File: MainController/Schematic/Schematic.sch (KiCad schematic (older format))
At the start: 3 parts

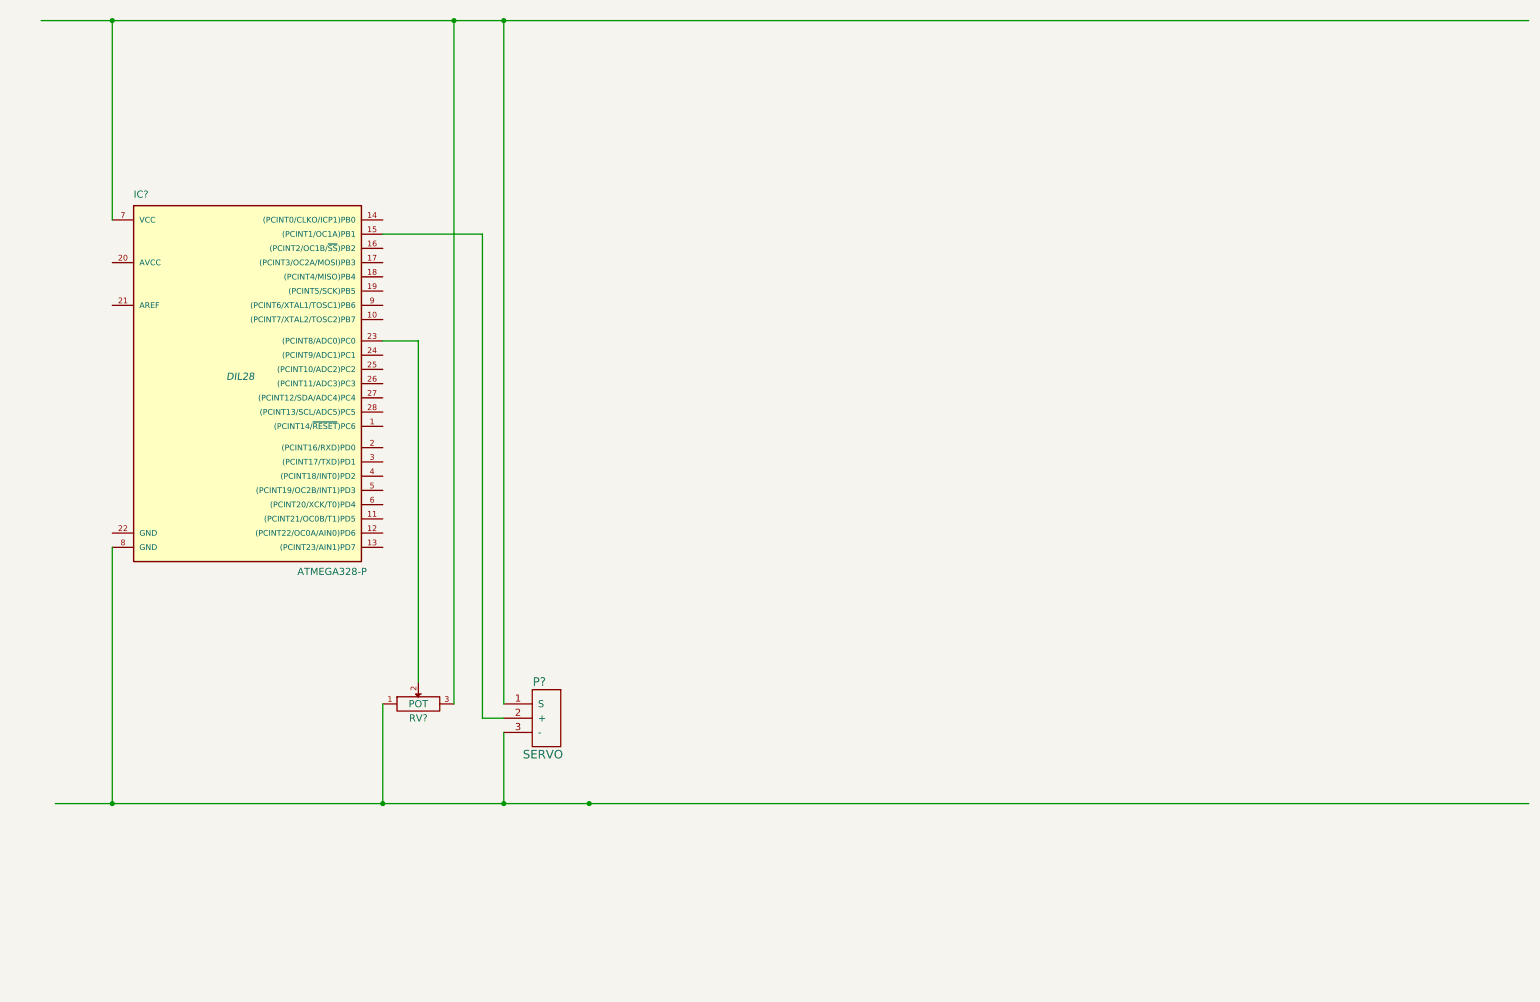
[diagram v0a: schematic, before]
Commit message: Updated Schematic
Added the push button and some LEDs currently used by the main
controllers programm. Also added bus lines for the SDA and SCL pins
required for I2C to work.
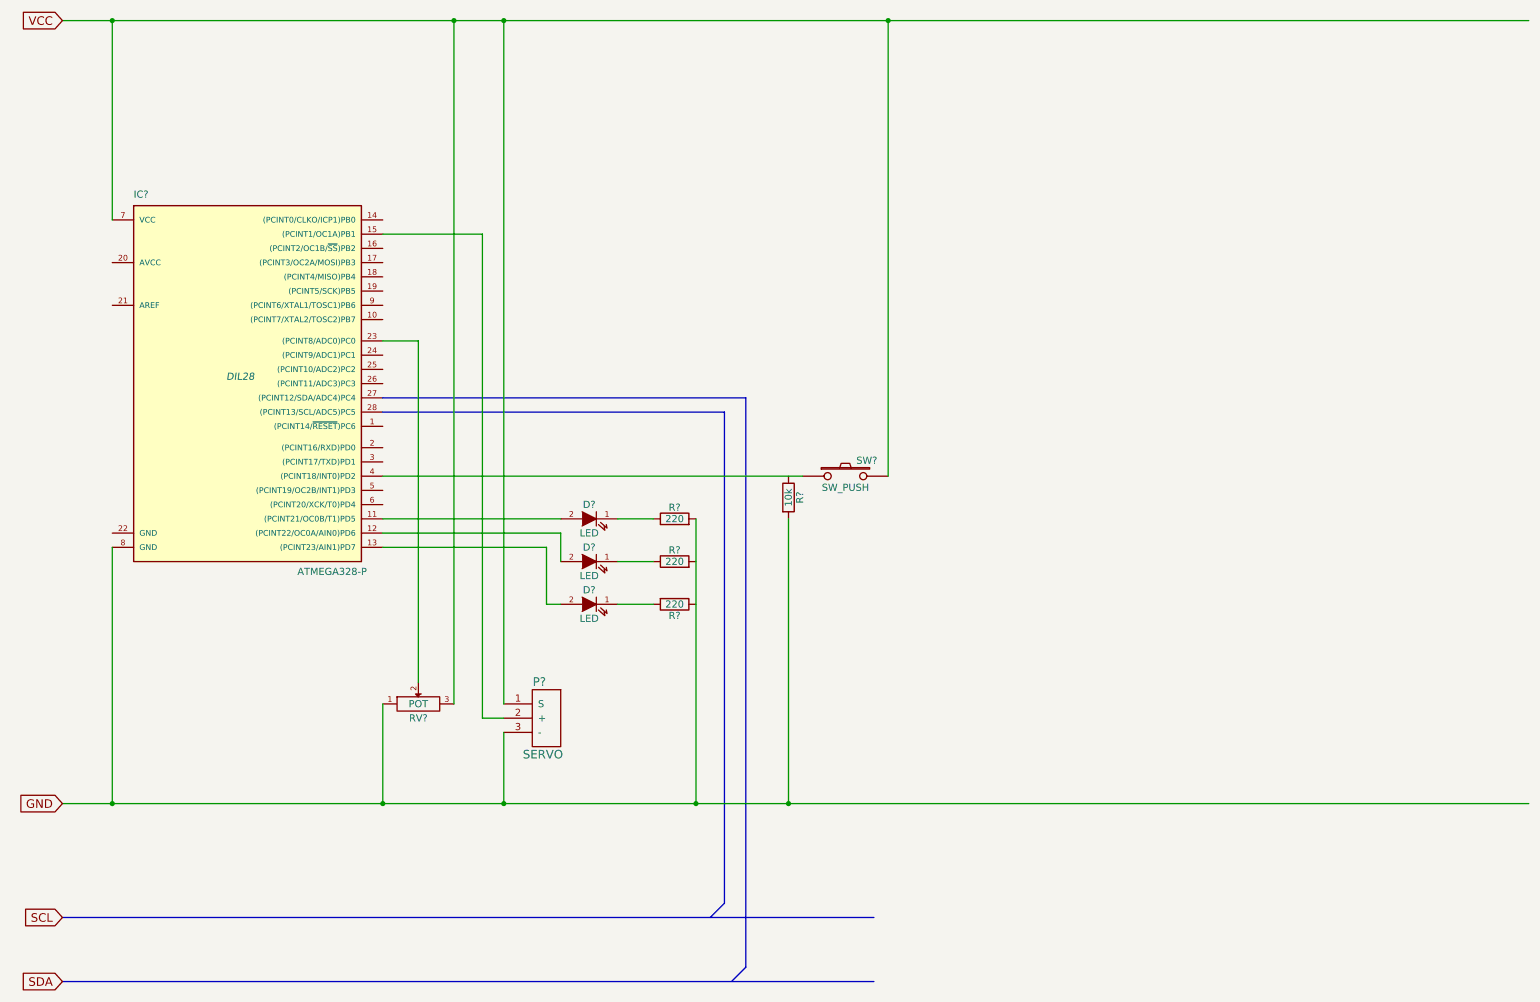
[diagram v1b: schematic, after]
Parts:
- added D? (x3): LED, symbol LED
- added R? (x3): 220, symbol R
- added R?: 10k, symbol R
- added SW?: SW_PUSH, symbol SW_PUSH
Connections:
- net labels added: GND, SCL, SDA, VCC
- wire segments 13 -> 26
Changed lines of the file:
@@
 LIBS:msp430
 LIBS:servo
-LIBS:Steuereinheit-cache
 EELAYER 25 0
 EELAYER END
@@
 $EndComp
 Wire Wire Line
-	750  6250 11100 6250
-Wire Wire Line
-	650  750  11100 750
+	800  6250 11100 6250
+Wire Wire Line
+	800  750  11100 750
 Wire Wire Line
 	1150 2150 1150 750
@@
 	1150 4450 1150 6250
 Connection ~ 1150 6250
-Connection ~ 4500 6250
 Wire Wire Line
 	3750 2250 3750 5650
@@
 	3750 2250 3050 2250
 Wire Wire Line
-	3900 5750 3900 6250
+	3900 6250 3900 5750
 Connection ~ 3900 6250
 Wire Wire Line
 	3900 5550 3900 750
 Connection ~ 3900 750
+$Comp
+L LED D?
+U 1 1 577E6E9D
+P 4500 4850
+F 0 "D?" H 4500 4950 50  0000 C CNN
+F 1 "LED" H 4500 4750 50  0000 C CNN
+F 2 "" H 4500 4850 50  0000 C CNN
+F 3 "" H 4500 4850 50  0000 C CNN
+	1    4500 4850
+	-1   0    0    -1
+$EndComp
+$Comp
+L LED D?
+U 1 1 577E6F7A
+P 4500 4550
+F 0 "D?" H 4500 4650 50  0000 C CNN
+F 1 "LED" H 4500 4450 50  0000 C CNN
+F 2 "" H 4500 4550 50  0000 C CNN
+F 3 "" H 4500 4550 50  0000 C CNN
+	1    4500 4550
+	-1   0    0    -1
+$EndComp
+$Comp
+L LED D?
+U 1 1 577E6FBD
+P 4500 4250
+F 0 "D?" H 4500 4350 50  0000 C CNN
+F 1 "LED" H 4500 4150 50  0000 C CNN
+F 2 "" H 4500 4250 50  0000 C CNN
+F 3 "" H 4500 4250 50  0000 C CNN
+	1    4500 4250
+	-1   0    0    -1
+$EndComp
+$Comp
+L R R?
+U 1 1 577E709E
+P 5100 4850
+F 0 "R?" V 5180 4850 50  0000 C CNN
+F 1 "220" V 5100 4850 50  0000 C CNN
+F 2 "" V 5030 4850 50  0000 C CNN
+F 3 "" H 5100 4850 50  0000 C CNN
+	1    5100 4850
+	0    1    1    0
+$EndComp
+$Comp
+L R R?
+U 1 1 577E71D5
+P 5100 4550
+F 0 "R?" V 5180 4550 50  0000 C CNN
+F 1 "220" V 5100 4550 50  0000 C CNN
+F 2 "" V 5030 4550 50  0000 C CNN
+F 3 "" H 5100 4550 50  0000 C CNN
+	1    5100 4550
+	0    -1   -1   0
+$EndComp
+$Comp
+L R R?
+U 1 1 577E721E
+P 5100 4250
+F 0 "R?" V 5180 4250 50  0000 C CNN
+F 1 "220" V 5100 4250 50  0000 C CNN
+F 2 "" V 5030 4250 50  0000 C CNN
+F 3 "" H 5100 4250 50  0000 C CNN
+	1    5100 4250
+	0    -1   -1   0
+$EndComp
+Wire Wire Line
+	3050 4250 4300 4250
+Wire Wire Line
+	4700 4250 4950 4250
+Wire Wire Line
+	5250 4250 5250 6250
+Connection ~ 5250 6250
+Wire Wire Line
+	3050 4350 4300 4350
+Wire Wire Line
+	4300 4350 4300 4550
+Wire Wire Line
+	4700 4550 4950 4550
+Wire Wire Line
+	4700 4850 4950 4850
+Wire Wire Line
+	3050 4450 4200 4450
+Wire Wire Line
+	4200 4450 4200 4850
+Wire Wire Line
+	4200 4850 4300 4850
+Wire Bus Line
+	800  7050 6500 7050
+Wire Bus Line
+	800  7500 6500 7500
+Wire Bus Line
+	3050 3500 5450 3500
+Entry Bus Bus
+	5350 7050 5450 6950
+Wire Bus Line
+	5450 3500 5450 6950
+Entry Bus Bus
+	5500 7500 5600 7400
+Wire Bus Line
+	3050 3400 5600 3400
+Wire Bus Line
+	5600 3400 5600 7400
+$Comp
+L SW_PUSH SW?
+U 1 1 577E8C5E
+P 6300 3950
+F 0 "SW?" H 6450 4060 50  0000 C CNN
+F 1 "SW_PUSH" H 6300 3870 50  0000 C CNN
+F 2 "" H 6300 3950 50  0000 C CNN
+F 3 "" H 6300 3950 50  0000 C CNN
+	1    6300 3950
+	1    0    0    -1
+$EndComp
+Wire Wire Line
+	3050 3950 6000 3950
+$Comp
+L R R?
+U 1 1 577E909C
+P 5900 4100
+F 0 "R?" V 5980 4100 50  0000 C CNN
+F 1 "10k" V 5900 4100 50  0000 C CNN
+F 2 "" V 5830 4100 50  0000 C CNN
+F 3 "" H 5900 4100 50  0000 C CNN
+	1    5900 4100
+	1    0    0    -1
+$EndComp
+Wire Wire Line
+	5900 4250 5900 6250
+Connection ~ 5900 6250
+Wire Wire Line
+	6600 3950 6600 750
+Connection ~ 6600 750
+Text GLabel 800  7500 0    60   Input ~ 0
+SDA
+Text GLabel 800  7050 0    60   Input ~ 0
+SCL
+Text GLabel 800  6250 0    60   Input ~ 0
+GND
+Text GLabel 800  750  0    60   Input ~ 0
+VCC
 $EndSCHEMATC
